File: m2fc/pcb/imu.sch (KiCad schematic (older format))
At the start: 49 parts

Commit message: update more bits on flight computer..
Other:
- note added: "Inertial Measurement Unit"
- moved on the sheet: C?, IC?, R?, TP?

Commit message: everything... wired... up...
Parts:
- added TP?: TESTPAD, symbol TESTPAD
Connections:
- net +3.3V: now also IC?.4 (I2C_LSB)
- net GYRO_INT1: now reaches IC?.7 (INT1)
- net GYRO_INT1: now also TP?.1 (TP)
- no-connect marks 2 -> 0
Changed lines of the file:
@@
 	1    0    0    -1
 $EndComp
-NoConn ~ 3800 4150
 $Comp
 L R R?
@@
 	1    0    0    -1
 $EndComp
-NoConn ~ 3800 4550
 Text Notes 2250 5200 0    60   ~ 0
 GYROSCOPE
@@
 L +3.3V #PWR068
 U 1 1 53B679BB
-P 3900 4250
-F 0 "#PWR068" H 3900 4210 30  0001 C CNN
-F 1 "+3.3V" H 3900 4360 30  0000 C CNN
-F 2 "" H 3900 4250 60  0000 C CNN
-F 3 "" H 3900 4250 60  0000 C CNN
-	1    3900 4250
+P 3950 4250
+F 0 "#PWR068" H 3950 4210 30  0001 C CNN
+F 1 "+3.3V" H 3950 4360 30  0000 C CNN
+F 2 "" H 3950 4250 60  0000 C CNN
+F 3 "" H 3950 4250 60  0000 C CNN
+	1    3950 4250
 	1    0    0    -1
 $EndComp
@@
 Connection ~ 3900 4050
 Wire Wire Line
-	3800 4250 3900 4250
+	3800 4250 3950 4250
 Wire Wire Line
 	3800 4450 4000 4450
@@
 Wire Notes Line
 	7450 5250 9400 5250
+Text HLabel 4000 4550 2    60   Output ~ 0
+GYRO_INT1
+Wire Wire Line
+	3800 4550 4000 4550
+$Comp
+L TESTPAD TP?
+U 1 1 53C45860
+P 3950 4550
+F 0 "TP?" H 3980 4510 30  0000 C CNN
+F 1 "TESTPAD" H 3950 4600 60  0001 C CNN
+F 2 "" H 3950 4550 60  0000 C CNN
+F 3 "" H 3950 4550 60  0000 C CNN
+	1    3950 4550
+	0    -1   -1   0
+$EndComp
+Connection ~ 3950 4550
+Wire Wire Line
+	3800 4150 3850 4150
+Wire Wire Line
+	3850 4150 3850 4250
+Connection ~ 3850 4250
 $EndSCHEMATC

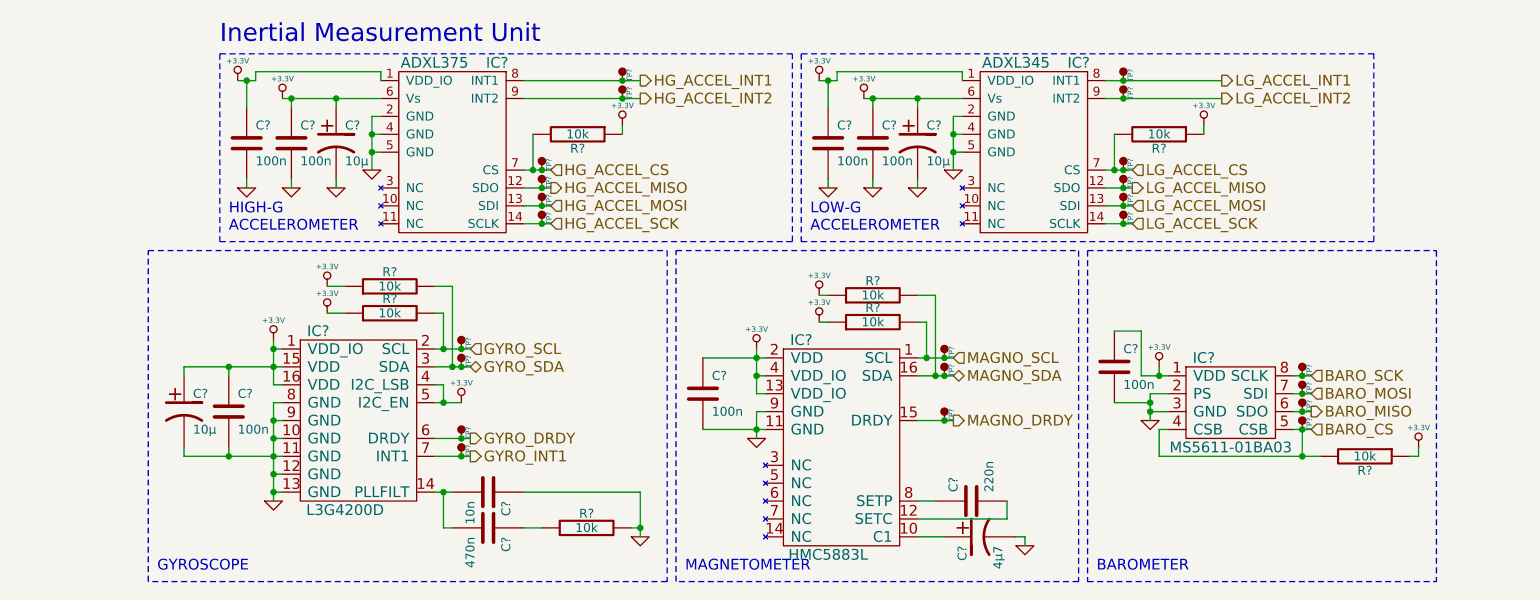
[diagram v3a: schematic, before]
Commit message: fix all the erc errors
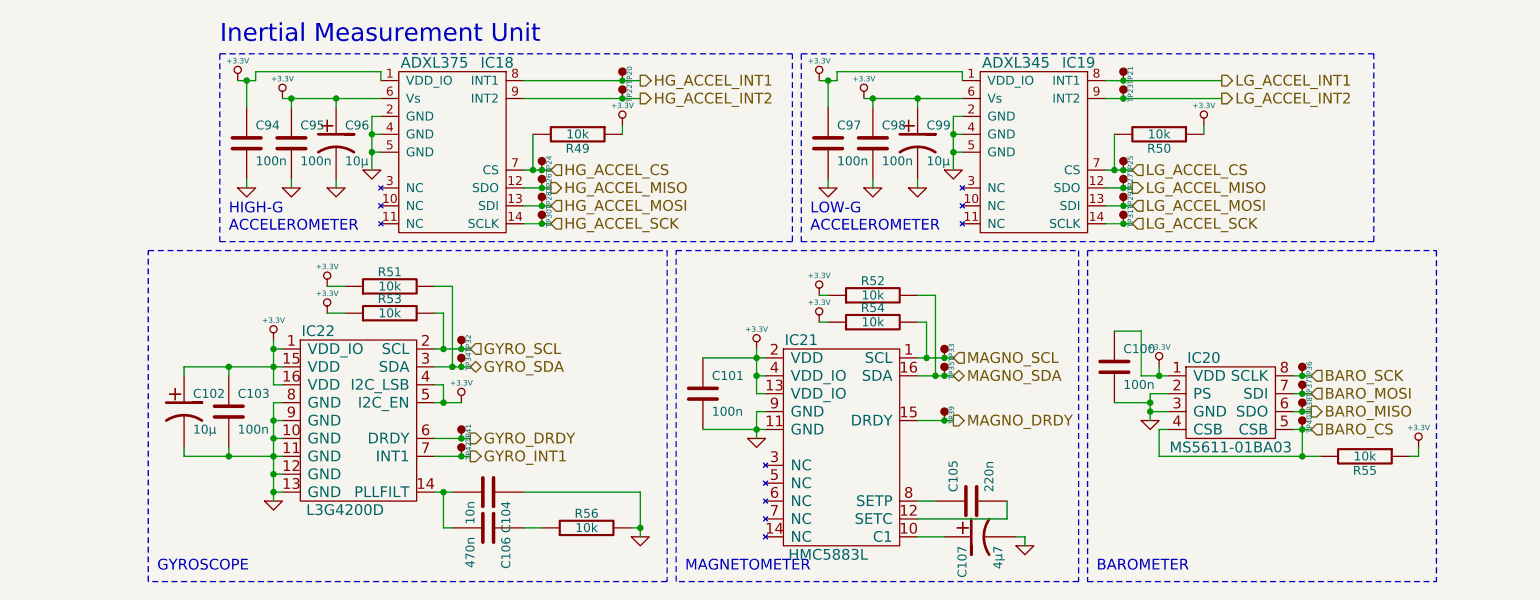
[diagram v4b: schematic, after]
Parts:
- removed IC?: L3G4200D, symbol L3G4200D
- added IC22: L3G4200D, symbol L3G4200D
- gave numbers to parts that had none: 49
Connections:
- net +3.3V: now also IC22.1 (VDD_IO), IC22.15 (VDD), IC22.16 (VDD), IC22.4 (I2C_LSB), IC22.5 (I2C_EN)
- net GND: now also IC22.10 (GND), IC22.11 (GND), IC22.12 (GND), IC22.13 (GND), IC22.8 (GND), IC22.9 (GND)
- net GYRO_DRDY: now also IC22.6 (DRDY)
- net GYRO_INT1: now also IC22.7 (INT1)
- net GYRO_SCL: now also IC22.2 (SCL)
- net GYRO_SDA: now also IC22.3 (SDA)
- net at C104.2, C106.2: now also IC22.14 (PLLFILT)

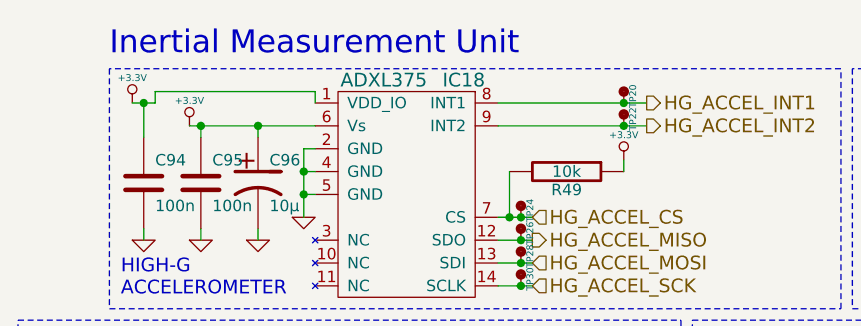
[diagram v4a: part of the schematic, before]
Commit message: consistent layout/typography
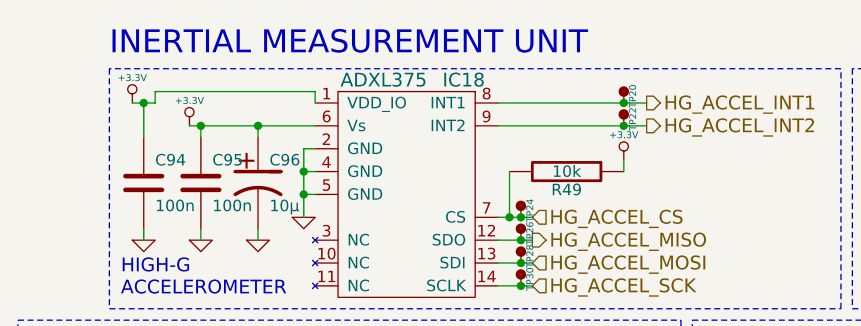
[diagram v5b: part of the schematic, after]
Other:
- note added: "INERTIAL MEASUREMENT UNIT"
- note removed: "Inertial Measurement Unit"
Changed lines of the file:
@@
 Connection ~ 6650 4000
 Text Notes 2600 2250 0    100  ~ 0
-Inertial Measurement Unit
+INERTIAL MEASUREMENT UNIT
 Wire Notes Line
 	7450 5250 9400 5250

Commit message: add missing farnell numbers
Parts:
- IC19: Farnell (none) -> 1853935
- IC22: Farnell (none) -> 1872924
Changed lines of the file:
@@
 F 2 "" H 6750 3250 60  0000 C CNN
 F 3 "" H 6750 3250 60  0000 C CNN
+F 4 "1853935" H 6750 3250 60  0001 C CNN "Farnell"
 	1    6750 3250
 	1    0    0    -1
@@
 F 2 "" H 3400 4450 60  0000 C CNN
 F 3 "" H 3400 4450 60  0000 C CNN
+F 4 "1872924" H 3400 4450 60  0001 C CNN "Farnell"
 	1    3400 4450
 	1    0    0    -1

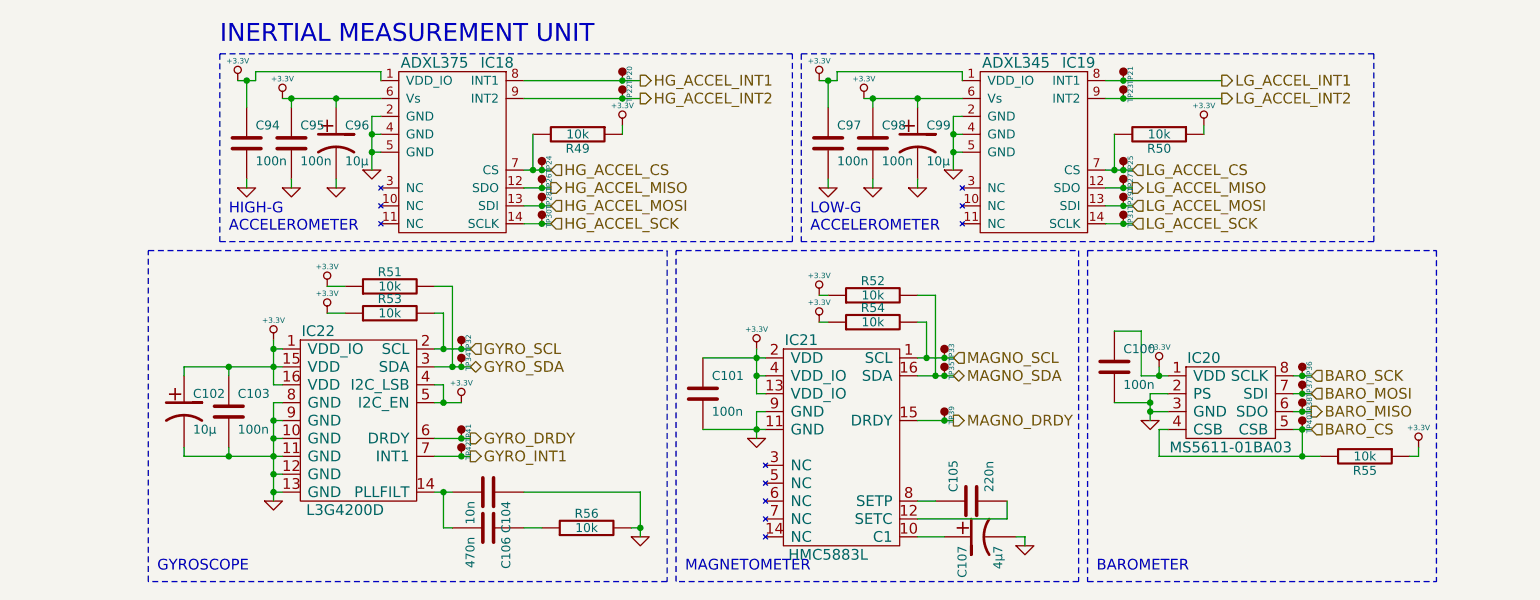
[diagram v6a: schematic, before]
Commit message: update m2fc sch with 3rd pyro and SJs
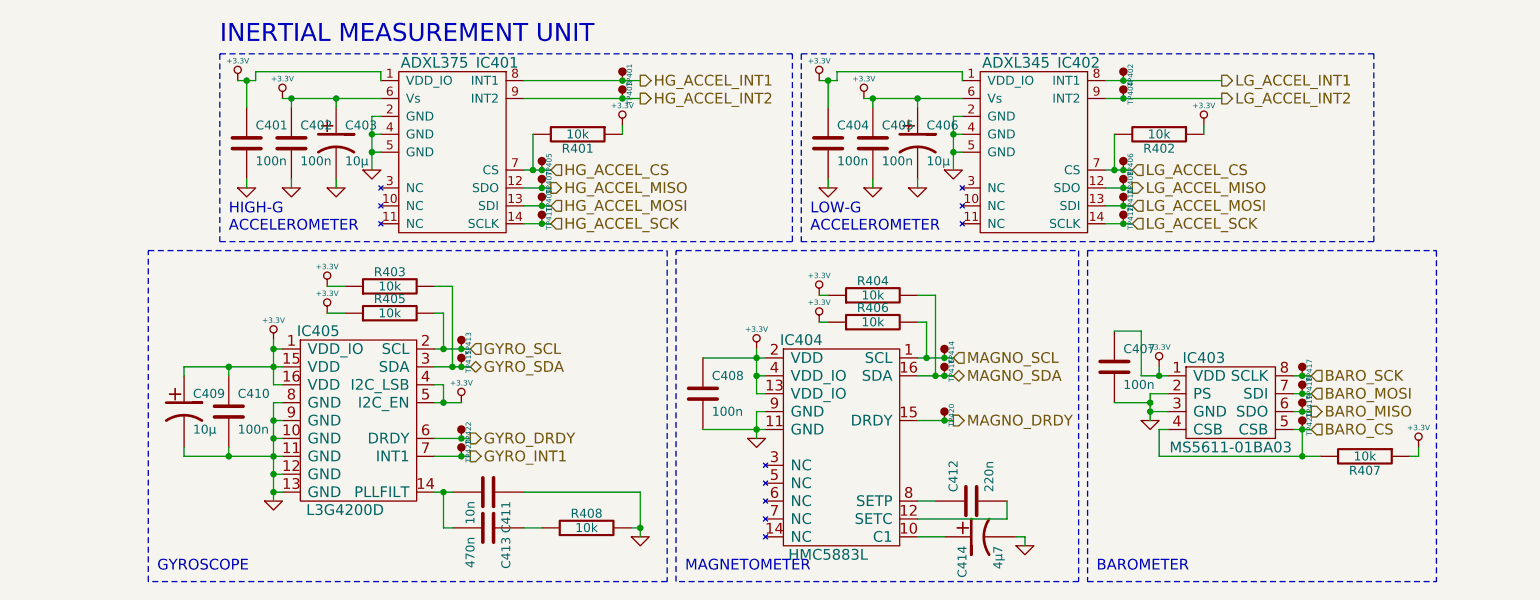
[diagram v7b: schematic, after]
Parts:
- renumbered C94 to C401, C95 to C402, C96 to C403, C97 to C404, C98 to C405, C99 to C406, C100 to C407, C101 to C408, C102 to C409, C103 to C410, C104 to C411, C105 to C412, C106 to C413, C107 to C414, IC18 to IC401, IC19 to IC402, IC20 to IC403, IC21 to IC404, IC22 to IC405, R49 to R401, R50 to R402, R51 to R403, R52 to R404, R53 to R405, R54 to R406, R55 to R407, R56 to R408, TP20 to TP401, TP21 to TP402, TP22 to TP403, TP23 to TP404, TP24 to TP405, TP25 to TP406, TP26 to TP407, TP27 to TP408, TP28 to TP409, TP29 to TP410, TP30 to TP411, TP31 to TP412, TP32 to TP413, TP33 to TP414, TP34 to TP415, TP35 to TP416, TP36 to TP417, TP37 to TP418, TP38 to TP419, TP39 to TP420, TP40 to TP421, TP41 to TP422, TP42 to TP423

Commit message: sd pullups, shielded sgs
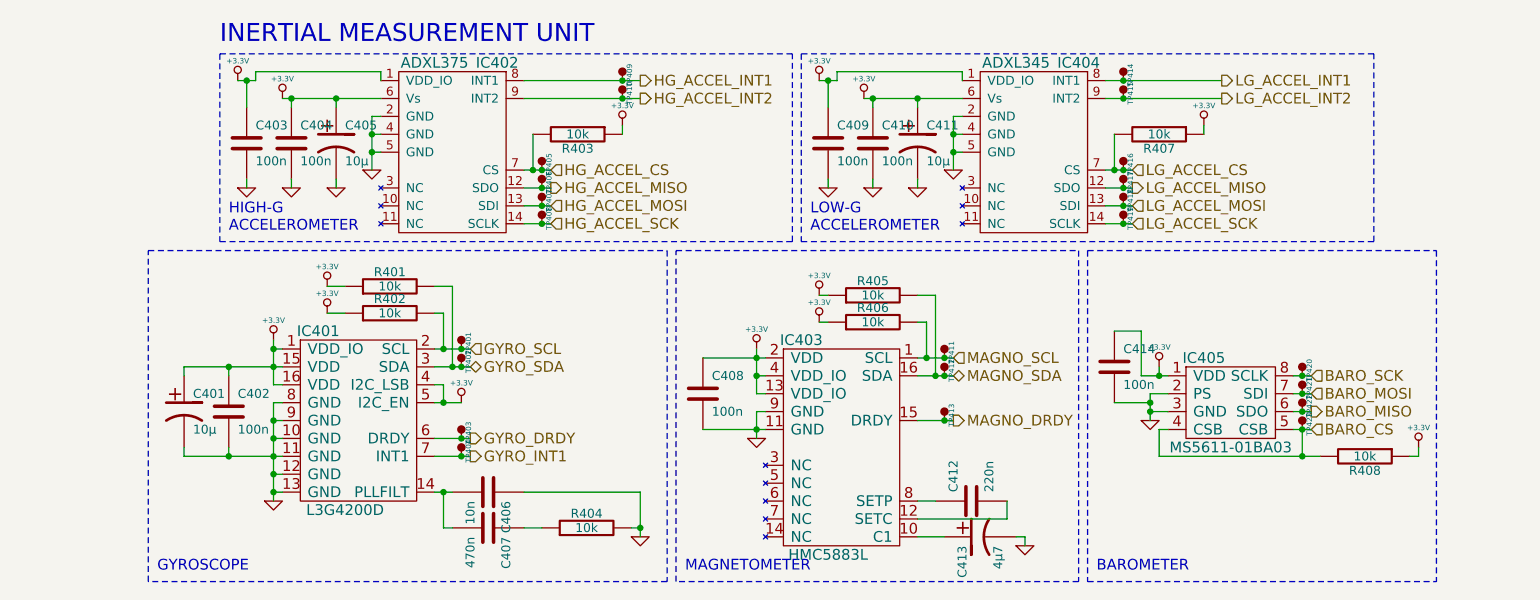
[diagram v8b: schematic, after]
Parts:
- C402: renamed from C410; footprint 0603 -> m2fc:C0603
- C403: renamed from C401; footprint 0603 -> m2fc:C0603
- C404: renamed from C402; footprint 0603 -> m2fc:C0603
- C406: renamed from C411; footprint 0603 -> m2fc:C0603
- C407: renamed from C413; footprint 0603 -> m2fc:C0603
- C408, C412: footprint 0603 -> m2fc:C0603
- C409: renamed from C404; footprint 0603 -> m2fc:C0603
- C410: renamed from C405; footprint 0603 -> m2fc:C0603
- C413: renamed from C414; footprint 0603 -> m2fc:C0603
- C414: renamed from C407; footprint 0603 -> m2fc:C0603
- R401: renamed from R403; footprint 0603 -> m2fc:R0603
- R402: renamed from R405; footprint 0603 -> m2fc:R0603
- R403: renamed from R401; footprint 0603 -> m2fc:R0603
- R404: renamed from R408; footprint 0603 -> m2fc:R0603
- R405: renamed from R404; footprint 0603 -> m2fc:R0603
- R406: footprint 0603 -> m2fc:R0603
- R407: renamed from R402; footprint 0603 -> m2fc:R0603
- R408: renamed from R407; footprint 0603 -> m2fc:R0603
- TP401: renamed from TP413; footprint (none) -> m2fc:TESTPAD
- TP402: renamed from TP415; footprint (none) -> m2fc:TESTPAD
- TP403: renamed from TP422; footprint (none) -> m2fc:TESTPAD
- TP404: renamed from TP423; footprint (none) -> m2fc:TESTPAD
- TP405: footprint (none) -> m2fc:TESTPAD
- TP406: renamed from TP407; footprint (none) -> m2fc:TESTPAD
- TP407: renamed from TP409; footprint (none) -> m2fc:TESTPAD
- TP408: renamed from TP411; footprint (none) -> m2fc:TESTPAD
- TP409: renamed from TP401; footprint (none) -> m2fc:TESTPAD
- TP410: renamed from TP403; footprint (none) -> m2fc:TESTPAD
- TP411: renamed from TP414; footprint (none) -> m2fc:TESTPAD
- TP412: renamed from TP416; footprint (none) -> m2fc:TESTPAD
- TP413: renamed from TP420; footprint (none) -> m2fc:TESTPAD
- TP414: renamed from TP402; footprint (none) -> m2fc:TESTPAD
- TP415: renamed from TP404; footprint (none) -> m2fc:TESTPAD
- TP416: renamed from TP406; footprint (none) -> m2fc:TESTPAD
- TP417: renamed from TP408; footprint (none) -> m2fc:TESTPAD
- TP418: renamed from TP410; footprint (none) -> m2fc:TESTPAD
- TP419: renamed from TP412; footprint (none) -> m2fc:TESTPAD
- TP420: renamed from TP417; footprint (none) -> m2fc:TESTPAD
- TP421: renamed from TP418; footprint (none) -> m2fc:TESTPAD
- TP422: renamed from TP419; footprint (none) -> m2fc:TESTPAD
- TP423: renamed from TP421; footprint (none) -> m2fc:TESTPAD
- renumbered C409 to C401, C403 to C405, C406 to C411, IC405 to IC401, IC401 to IC402, IC404 to IC403, IC402 to IC404, IC403 to IC405
